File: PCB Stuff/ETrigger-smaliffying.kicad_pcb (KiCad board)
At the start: 2 copper layers, 42.2 x 27.4 mm, 45 parts, among them IC1 ATTINY85-S, IC2 A1302KUA-T, P2 CONN_01X04, P3 CONN_01X01, SW1 SW_DIP_x01, SW2 SW_DIP_x01, U4 LMV331, U5 Fan3100

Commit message: Fixed Mistake
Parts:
- added REF**: C_1206_HandSoldering, Capacitors_SMD:C_1206_HandSoldering, F.Cu at (154.3, 115.1)
- moved 10uF 0.29 mm to (142.1, 113.4)
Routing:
- net GND: track 36.8 -> 40.2 mm, vias 10 -> 11
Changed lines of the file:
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@@
 (kicad_pcb (version 4) (host pcbnew 4.0.5)
   (general
-    (links 76)
+    (links 78)
     (no_connects 0)
     (area 120.400203 105.918 171.098534 144.208501)
     (thickness 1.6)
     (drawings 108)
-    (tracks 179)
+    (tracks 186)
     (zones 0)
-    (modules 45)
+    (modules 46)
     (nets 15)
   )
@@
     (mod_text_size 1 1)
     (mod_text_width 0.15)
-    (pad_size 2 0.65)
+    (pad_size 2 1.6)
     (pad_drill 0)
     (pad_to_mask_clearance 0)
@@
   )
   (module Capacitors_SMD:C_0805_HandSoldering (layer F.Cu)
-    (at 142.113 113.0735 90)
+    (at 142.113 113.3675 90)
     (descr "Capacitor SMD 0805, hand soldering")
     (tags "capacitor 0805")
@@
     )
   )
+  (module Capacitors_SMD:C_1206_HandSoldering (layer F.Cu)
+    (at 154.273 115.062)
+    (descr "Capacitor SMD 1206, hand soldering")
+    (tags "capacitor 1206")
+    (attr smd)
+    (fp_text reference REF** (at 0.6985 -4.0005) (layer F.SilkS)
+      (effects (font (size 1 1) (thickness 0.15)))
+    )
+    (fp_text value C_1206_HandSoldering (at 0 2) (layer F.Fab)
+      (effects (font (size 1 1) (thickness 0.15)))
+    )
+    (fp_text user %R (at 0 -1.75) (layer F.Fab)
+      (effects (font (size 1 1) (thickness 0.15)))
+    )
+    (fp_line (start -1.6 0.8) (end -1.6 -0.8) (layer F.Fab) (width 0.1))
+    (fp_line (start 1.6 0.8) (end -1.6 0.8) (layer F.Fab) (width 0.1))
+    (fp_line (start 1.6 -0.8) (end 1.6 0.8) (layer F.Fab) (width 0.1))
+    (fp_line (start -1.6 -0.8) (end 1.6 -0.8) (layer F.Fab) (width 0.1))
+    (fp_line (start 1 -1.02) (end -1 -1.02) (layer F.SilkS) (width 0.12))
+    (fp_line (start -1 1.02) (end 1 1.02) (layer F.SilkS) (width 0.12))
+    (fp_line (start -3.25 -1.05) (end 3.25 -1.05) (layer F.CrtYd) (width 0.05))
+    (fp_line (start -3.25 -1.05) (end -3.25 1.05) (layer F.CrtYd) (width 0.05))
+    (fp_line (start 3.25 1.05) (end 3.25 -1.05) (layer F.CrtYd) (width 0.05))
+    (fp_line (start 3.25 1.05) (end -3.25 1.05) (layer F.CrtYd) (width 0.05))
+    (pad 1 smd rect (at -2 0) (size 2 1.6) (layers F.Cu F.Paste F.Mask)
+      (net 3 +5V))
+    (pad 2 smd rect (at 2 0) (size 2 1.6) (layers F.Cu F.Paste F.Mask)
+      (net 2 GND))
+    (model Capacitors_SMD.3dshapes/C_1206.wrl
+      (at (xyz 0 0 0))
+      (scale (xyz 1 1 1))
+      (rotate (xyz 0 0 0))
+    )
+  )
   (gr_line (start 163.97644 110.1988) (end 156.70415 110.1988) (layer Eco1.User) (width 0.1))
   (gr_arc (start 163.97644 130.75204) (end 164.97644 130.75204) (angle 85.62273379) (layer Eco1.User) (width 0.1))
@@
   (gr_arc (start 131.028992 122.047922) (end 131.028992 121.047922) (angle -105) (layer Edge.Cuts) (width 0.1))
   (gr_arc (start 129.12344 126.7206) (end 129.058735 126.479118) (angle -90) (layer Edge.Cuts) (width 0.1))
+  (segment (start 149.126 119.228) (end 149.167929 119.228) (width 0.75) (layer F.Cu) (net 1))
+  (segment (start 149.167929 119.228) (end 151.13 121.190071) (width 0.75) (layer F.Cu) (net 1))
+  (segment (start 151.13 121.190071) (end 151.13 121.666) (width 0.75) (layer F.Cu) (net 1))
+  (segment (start 151.13 121.666) (end 150.876 121.666) (width 0.75) (layer F.Cu) (net 1))
+  (segment (start 150.876 121.666) (end 149.838521 122.703479) (width 0.75) (layer F.Cu) (net 1))
+  (segment (start 149.838521 122.703479) (end 149.838521 128.487803) (width 0.75) (layer F.Cu) (net 1))
+  (segment (start 149.838521 128.487803) (end 148.024324 130.302) (width 0.75) (layer F.Cu) (net 1))
+  (segment (start 148.024324 130.302) (end 147.0025 130.302) (width 0.75) (layer F.Cu) (net 1))
   (segment (start 139.4805 125.0985) (end 138.9055 124.5235) (width 0.25) (layer F.Cu) (net 1))
   (segment (start 142.347001 126.803001) (end 140.185459 126.803) (width 0.25) (layer F.Cu) (net 1))
@@
   (segment (start 144.980518 126.111) (end 144.145 126.111) (width 0.75) (layer F.Cu) (net 1))
   (segment (start 144.145 126.111) (end 143.637 125.603) (width 0.75) (layer F.Cu) (net 1))
-  (segment (start 151.13 120.82533) (end 151.13 121.666) (width 0.75) (layer F.Cu) (net 1))
-  (segment (start 149.838521 128.487803) (end 149.838521 122.703479) (width 0.75) (layer F.Cu) (net 1))
-  (segment (start 149.53267 119.228) (end 151.13 120.82533) (width 0.75) (layer F.Cu) (net 1))
-  (segment (start 149.838521 122.703479) (end 150.876 121.666) (width 0.75) (layer F.Cu) (net 1))
-  (segment (start 149.126 119.228) (end 149.53267 119.228) (width 0.75) (layer F.Cu) (net 1))
-  (segment (start 150.876 121.666) (end 151.13 121.666) (width 0.75) (layer F.Cu) (net 1))
-  (segment (start 148.024324 130.302) (end 149.838521 128.487803) (width 0.75) (layer F.Cu) (net 1))
-  (segment (start 147.0025 130.302) (end 148.024324 130.302) (width 0.75) (layer F.Cu) (net 1))
   (segment (start 147.0025 128.132982) (end 144.980518 126.111) (width 0.75) (layer F.Cu) (net 1))
   (segment (start 147.0025 130.302) (end 147.0025 128.132982) (width 0.75) (layer F.Cu) (net 1))
   (segment (start 149.339716 119.190096) (end 149.063681 119.190096) (width 0.75) (layer F.Cu) (net 1))
+  (segment (start 144.487466 121.558663) (end 144.799663 121.558663) (width 0.75) (layer F.Cu) (net 2))
+  (segment (start 144.799663 121.558663) (end 146.2405 122.9995) (width 0.75) (layer F.Cu) (net 2))
+  (via (at 146.2405 122.9995) (size 0.6) (drill 0.4) (layers F.Cu B.Cu) (net 2))
+  (segment (start 144.487466 121.134399) (end 144.487466 121.558663) (width 0.75) (layer F.Cu) (net 2))
+  (segment (start 144.487466 119.266534) (end 144.487466 121.134399) (width 0.75) (layer F.Cu) (net 2))
+  (segment (start 144.526 119.228) (end 144.487466 119.266534) (width 0.75) (layer F.Cu) (net 2))
+  (segment (start 142.113399 112.142455) (end 141.794444 111.8235) (width 0.75) (layer F.Cu) (net 2))
+  (segment (start 141.794444 111.8235) (end 141.0335 111.8235) (width 0.75) (layer F.Cu) (net 2))
+  (segment (start 156.273 115.062) (end 154.94 115.062) (width 0.75) (layer F.Cu) (net 2))
+  (via (at 154.94 115.062) (size 0.6) (drill 0.4) (layers F.Cu B.Cu) (net 2))
   (segment (start 139.954 111.8235) (end 137.795 111.8235) (width 0.75) (layer F.Cu) (net 2))
   (segment (start 140.021751 124.345683) (end 140.021751 124.070214) (width 0.5) (layer F.Cu) (net 2))
@@
   (segment (start 138.2305 123.5735) (end 139.9805 123.5735) (width 0.5) (layer F.Cu) (net 2))
   (segment (start 141.137 125.603) (end 141.137 125.528776) (width 0.75) (layer F.Cu) (net 2))
-  (segment (start 142.113 111.8235) (end 141.0335 111.8235) (width 0.75) (layer F.Cu) (net 2))
   (segment (start 139.954 111.8235) (end 141.0335 111.8235) (width 0.75) (layer F.Cu) (net 2))
   (via (at 141.0335 111.8235) (size 0.6) (drill 0.4) (layers F.Cu B.Cu) (net 2))
@@
   (segment (start 142.621 129.5795) (end 143.232 129.5795) (width 0.75) (layer F.Cu) (net 2))
   (segment (start 143.232 129.5795) (end 143.9545 130.302) (width 0.75) (layer F.Cu) (net 2))
-  (segment (start 144.526 119.228) (end 144.526 121.9835) (width 0.75) (layer F.Cu) (net 2))
-  (via (at 144.526 121.9835) (size 0.6) (drill 0.4) (layers F.Cu B.Cu) (net 2))
   (segment (start 151.638 119.948701) (end 151.615213 119.971488) (width 0.25) (layer F.Cu) (net 2))
   (segment (start 151.638 118.7215) (end 151.638 119.948701) (width 0.25) (layer F.Cu) (net 2))
@@
   (segment (start 164.574504 124.43841) (end 164.0332 123.897106) (width 0.25) (layer F.Cu) (net 5))
   (segment (start 164.0332 123.897106) (end 164.0332 123.19) (width 0.25) (layer F.Cu) (net 5))
+  (segment (start 162.11042 130.302) (end 162.17646 130.36804) (width 0.25) (layer F.Cu) (net 6))
   (segment (start 161.036 130.302) (end 162.11042 130.302) (width 0.25) (layer F.Cu) (net 6))
-  (segment (start 162.11042 130.302) (end 162.17646 130.36804) (width 0.25) (layer F.Cu) (net 6))
   (segment (start 161.104958 123.578242) (end 161.104958 130.233042) (width 0.25) (layer B.Cu) (net 6))
   (via (at 161.036 130.302) (size 0.6) (drill 0.4) (layers F.Cu B.Cu) (net 6))
@@
   (segment (start 158.1785 121.6139) (end 158.0096 121.7828) (width 0.25) (layer F.Cu) (net 14))
   (via (at 158.1785 121.0945) (size 0.6) (drill 0.4) (layers F.Cu B.Cu) (net 14))
+  (zone (net 3) (net_name +5V) (layer B.Cu) (hatch edge 0.508)
+    (priority 100)
+    (connect_pads yes (clearance 0.16))
+    (min_thickness 0.254)
+    (fill yes (arc_segments 16) (thermal_gap 0.508) (thermal_bridge_width 0.508) (smoothing fillet))
+    (polygon
+      (pts
+        (xy 143.4465 122.2375) (xy 150.3045 122.174) (xy 150.3045 110.744) (xy 143.1925 110.744) (xy 143.1925 122.2375)
+      )
+    )
+  )
   (zone (net 3) (net_name +5V) (layer F.Cu) (hatch edge 0.508)
     (connect_pads (clearance 0.16))
     (min_thickness 0.254)
-    (fill yes (arc_segments 16) (thermal_gap 0.508) (thermal_bridge_width 0.508))
+    (fill yes (arc_segments 16) (thermal_gap 0.508) (thermal_bridge_width 0.508) (smoothing chamfer) (radius 1))
     (polygon
       (pts
@@
     (polygon
       (pts
-        (xy 121.225703 105.918) (xy 169.231703 107.1245) (xy 163.072203 141.224) (xy 120.400203 138.43)
+        (xy 121.202011 105.892144) (xy 169.208011 107.098644) (xy 163.048511 141.198144) (xy 120.376511 138.404144)
       )
     )
-  )
-  (zone (net 3) (net_name +5V) (layer B.Cu) (hatch edge 0.508)
-    (priority 100)
-    (connect_pads yes (clearance 0.16))
-    (min_thickness 0.254)
-    (fill yes (arc_segments 16) (thermal_gap 0.508) (thermal_bridge_width 0.508) (smoothing fillet))
-    (polygon
-      (pts
-        (xy 143.5735 121.4755) (xy 150.4315 121.412) (xy 150.4315 109.982) (xy 143.3195 109.982) (xy 143.3195 121.4755)
-      )
-    )

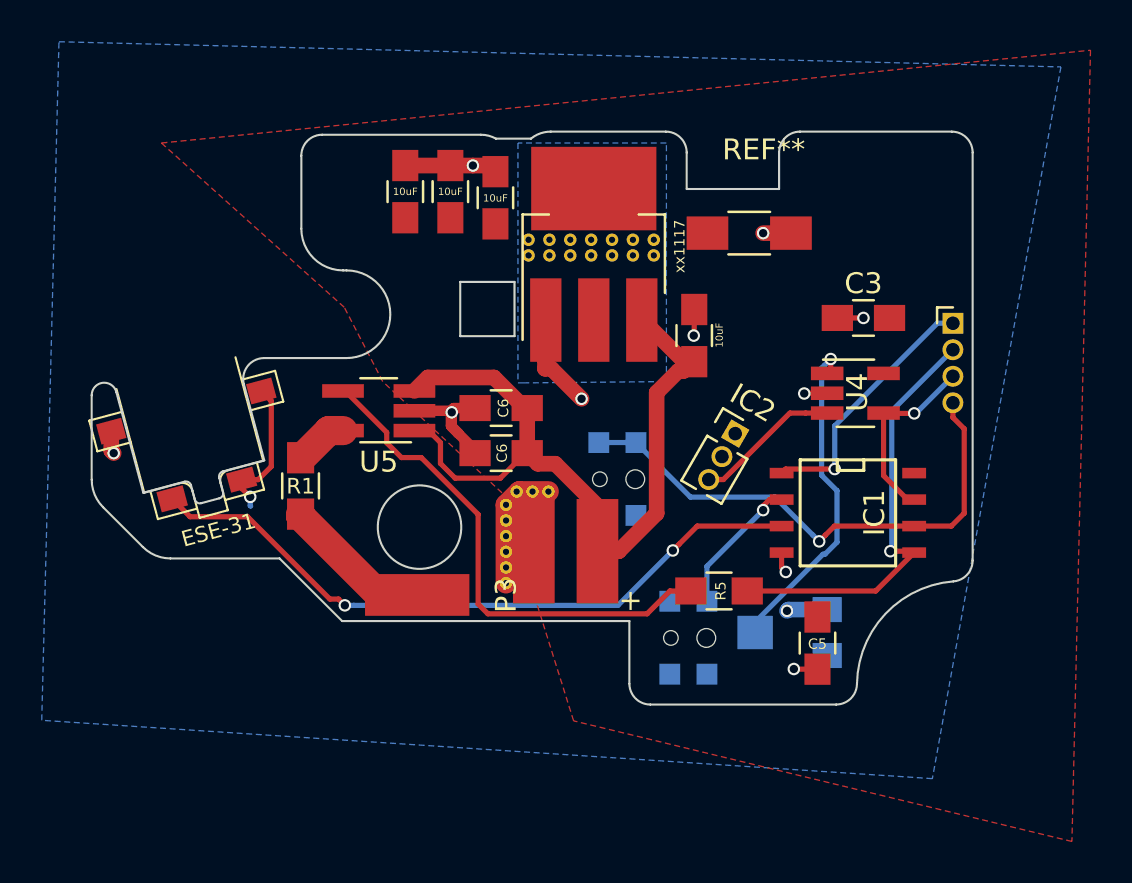
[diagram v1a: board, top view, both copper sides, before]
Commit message: Re-adding PCB stuff
I relaid out the board all components should be correct but we will see.
I left the reset pin floating on the attiny hopefully it doesnt caue any
troubles ill probably add an external pullup to it.
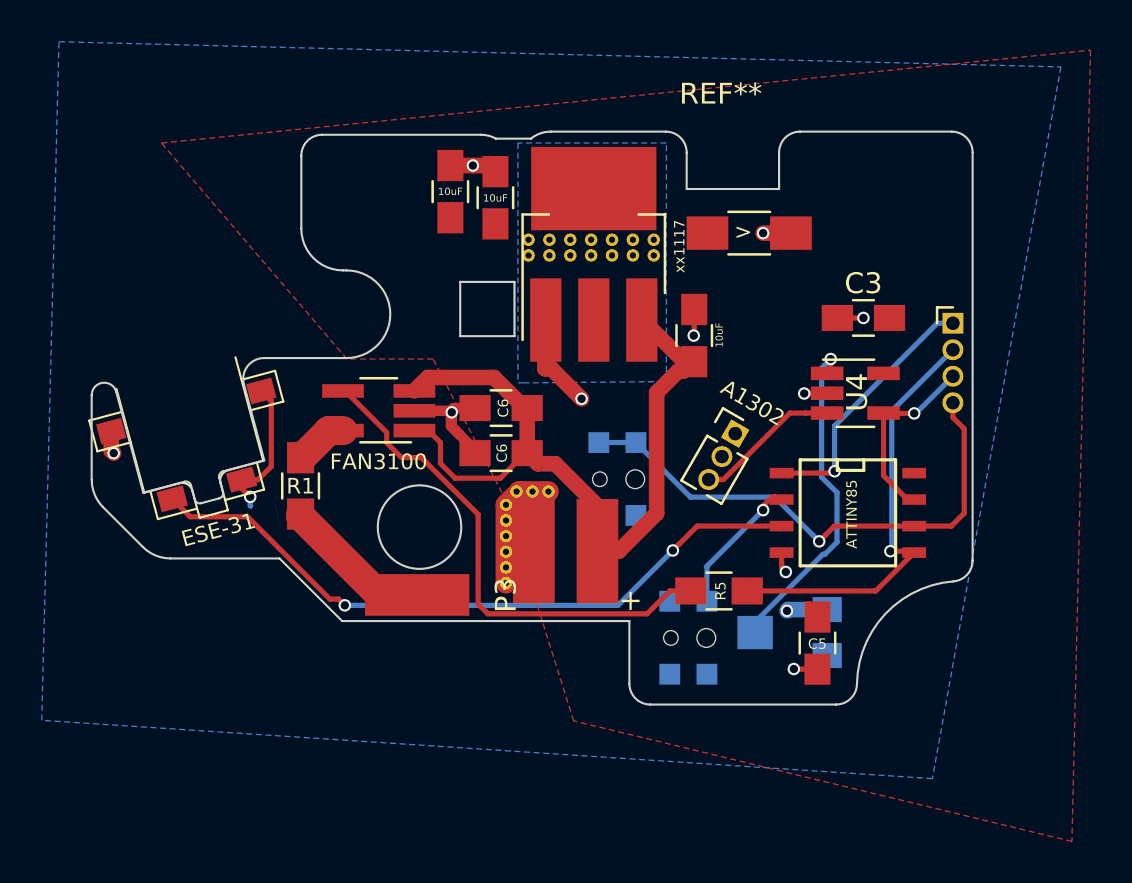
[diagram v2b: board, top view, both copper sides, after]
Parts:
- removed the 10uF at (137.8, 113.1)
- renumbered IC2 to A1302, IC1 to ATTINY85, U5 to FAN3100, SW2 to HDT001, SW1 to HDT001
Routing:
- net GND: track 40.2 -> 38.0 mm
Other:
- board text added: ">"
- board text added: "OpenETU By David Schallock An Open Source Electronic Trigger Unit"
- board text added: "OpenETU V3"
- board text added: "https://github.com/Davschall/OpenETU"

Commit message: Changed a few footprints
Messed up a footprint for a switch that is used upside down, I had it
mirrored, fixed that and made the attiny pads a little more hand
solderable.
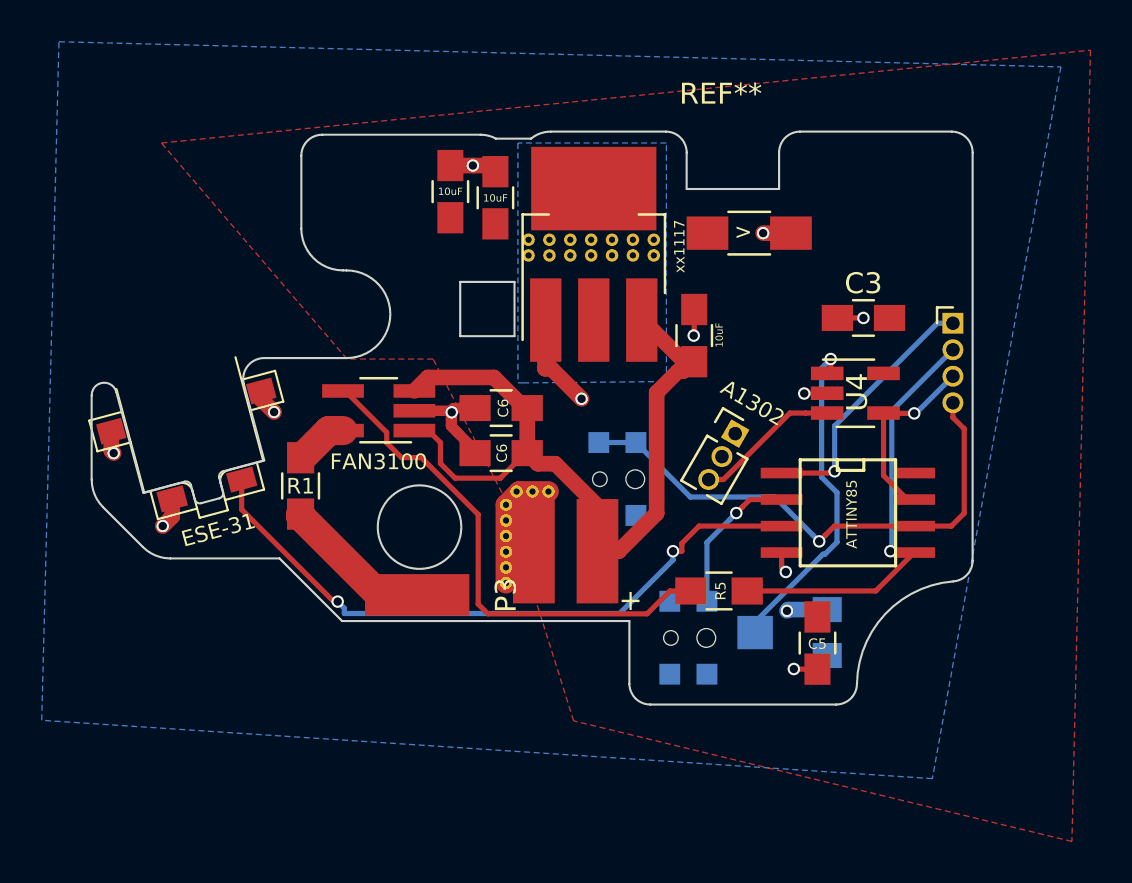
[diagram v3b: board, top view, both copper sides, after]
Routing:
- net GND: track 38.0 -> 33.8 mm, vias 11 -> 12
- net Cutoff: track 33.0 -> 31.7 mm
- net Net-(IC1-Pad2): track 8.47 -> 9.03 mm
